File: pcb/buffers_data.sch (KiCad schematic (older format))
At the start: 8 parts, among them U1 74LVCH162245A, U2 74LVCH162245A

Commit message: testpoints footprints added, some footprints assigned
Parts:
- R1, R2: footprint (none) -> Resistor_SMD:R_0603_1608Metric_Pad1.05x0.95mm_HandSolder
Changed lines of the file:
@@
 F 0 "R1" V 3043 6600 50  0000 C CNN
 F 1 "4.7k" V 3134 6600 50  0000 C CNN
-F 2 "" V 3180 6600 50  0001 C CNN
+F 2 "Resistor_SMD:R_0603_1608Metric_Pad1.05x0.95mm_HandSolder" V 3180 6600 50  0001 C CNN
 F 3 "~" H 3250 6600 50  0001 C CNN
 	1    3250 6600
@@
 F 0 "R2" V 3043 7100 50  0000 C CNN
 F 1 "4.7k" V 3134 7100 50  0000 C CNN
-F 2 "" V 3180 7100 50  0001 C CNN
+F 2 "Resistor_SMD:R_0603_1608Metric_Pad1.05x0.95mm_HandSolder" V 3180 7100 50  0001 C CNN
 F 3 "~" H 3250 7100 50  0001 C CNN
 	1    3250 7100

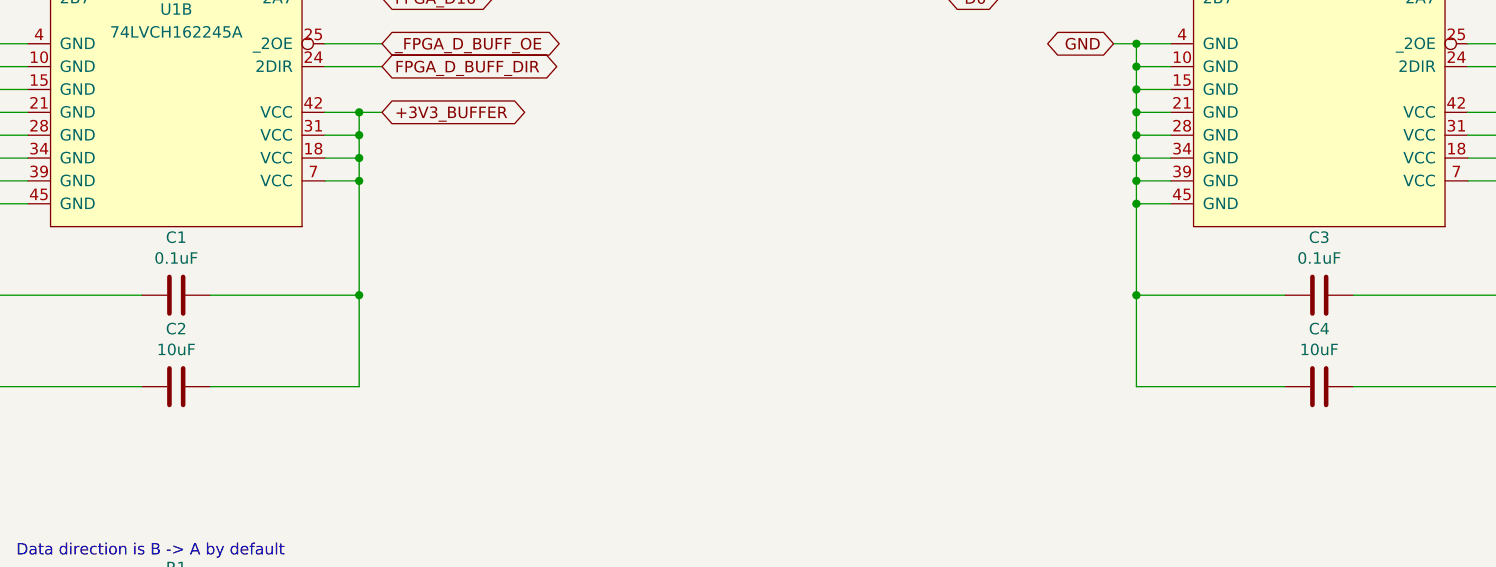
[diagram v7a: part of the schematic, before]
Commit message: more footprints assigned
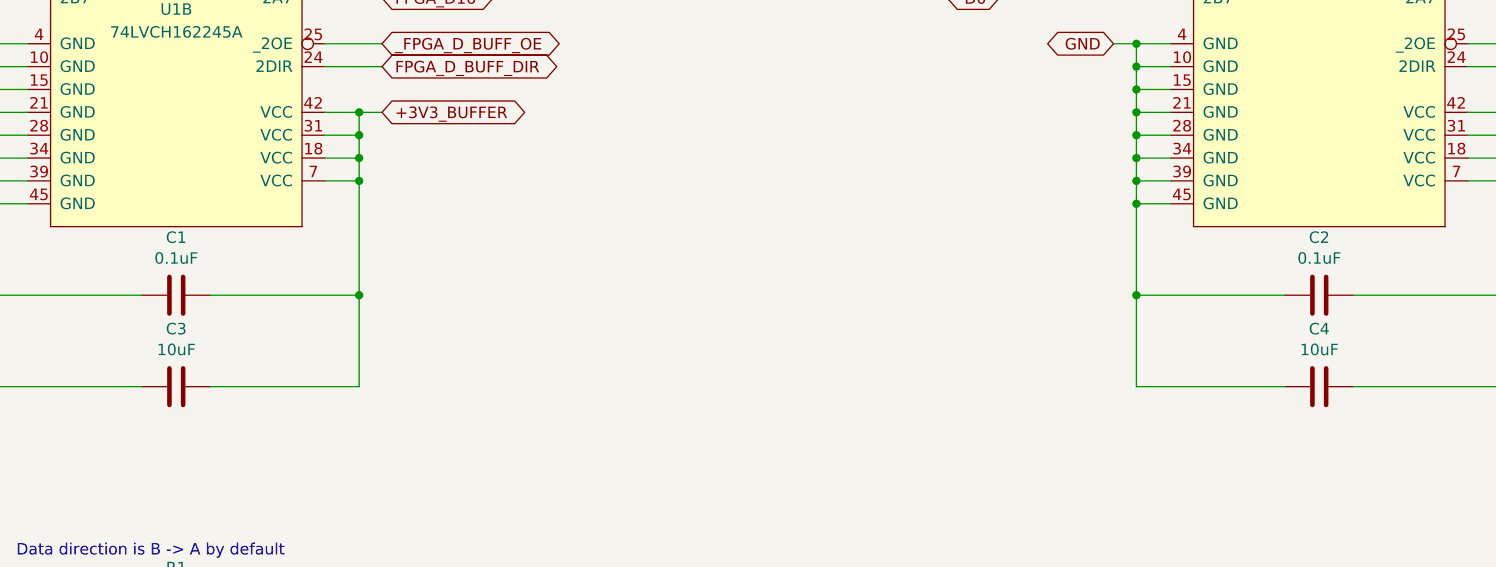
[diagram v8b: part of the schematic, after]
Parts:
- U1, U2: footprint (none) -> Package_SO:TSSOP-48_6.1x12.5mm_P0.5mm
- renumbered C3 to C2, C2 to C3
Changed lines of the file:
@@
 F 0 "U1" H 3250 3200 50  0000 C CNN
 F 1 "74LVCH162245A" H 3250 3100 50  0000 C CNN
-F 2 "" H 3250 2750 50  0001 C CNN
+F 2 "Package_SO:TSSOP-48_6.1x12.5mm_P0.5mm" H 3250 2750 50  0001 C CNN
 F 3 "" H 3250 2750 50  0001 C CNN
 	1    3250 2750
@@
 F 0 "U1" H 3250 5850 50  0000 C CNN
 F 1 "74LVCH162245A" H 3250 5750 50  0000 C CNN
-F 2 "" H 3250 4900 50  0001 C CNN
+F 2 "Package_SO:TSSOP-48_6.1x12.5mm_P0.5mm" H 3250 4900 50  0001 C CNN
 F 3 "" H 3250 4900 50  0001 C CNN
 	2    3250 4900
@@
 F 0 "U2" H 8250 3250 50  0000 C CNN
 F 1 "74LVCH162245A" H 8250 3150 50  0000 C CNN
-F 2 "" H 8250 2750 50  0001 C CNN
+F 2 "Package_SO:TSSOP-48_6.1x12.5mm_P0.5mm" H 8250 2750 50  0001 C CNN
 F 3 "" H 8250 2750 50  0001 C CNN
 	1    8250 2750
@@
 F 0 "U2" H 8250 6165 50  0000 C CNN
 F 1 "74LVCH162245A" H 8250 6074 50  0000 C CNN
-F 2 "" H 8250 4900 50  0001 C CNN
+F 2 "Package_SO:TSSOP-48_6.1x12.5mm_P0.5mm" H 8250 4900 50  0001 C CNN
 F 3 "" H 8250 4900 50  0001 C CNN
 	2    8250 4900
@@
 	8900 4600 9050 4600
 $Comp
-L Device:C C2
+L Device:C C3
 U 1 1 5E91F423
 P 3250 5600
-F 0 "C2" V 3502 5600 50  0000 C CNN
+F 0 "C3" V 3502 5600 50  0000 C CNN
 F 1 "10uF" V 3411 5600 50  0000 C CNN
 F 2 "" H 3288 5450 50  0001 C CNN
@@
 $EndComp
 $Comp
-L Device:C C3
+L Device:C C2
 U 1 1 5E79CB2C
 P 8250 5200
-F 0 "C3" V 8502 5200 50  0000 C CNN
+F 0 "C2" V 8502 5200 50  0000 C CNN
 F 1 "0.1uF" V 8411 5200 50  0000 C CNN
 F 2 "" H 8288 5050 50  0001 C CNN
